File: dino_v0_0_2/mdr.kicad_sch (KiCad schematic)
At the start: 12 parts, among them SW2 SW_Push, SW3 SW_Push, U18 74LS373, U22 74LS121, U23 74LS244N, U25 74LS245, U34 74LS373, U36 74LS73, U37 74LS04, U38 74LS02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

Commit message: Schematic Update
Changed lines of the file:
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@@
 	)
 	(junction
+		(at 125.73 78.74)
+		(diameter 0)
+		(color 0 0 0 0)
+	)
+	(junction
 		(at 194.31 26.67)
 		(diameter 0)
@@
 	)
 	(junction
-		(at 240.03 72.39)
-		(diameter 0)
-		(color 0 0 0 0)
-	)
-	(junction
 		(at 115.57 78.74)
 		(diameter 0)
@@
 	)
 	(junction
-		(at 186.69 132.08)
-		(diameter 0)
-		(color 0 0 0 0)
-	)
-	(junction
 		(at 83.82 105.41)
 		(diameter 0)
@@
 	)
 	(junction
-		(at 173.99 26.67)
+		(at 128.27 41.91)
 		(diameter 0)
 		(color 0 0 0 0)
 	)
 	(junction
-		(at 128.27 41.91)
+		(at 203.2 76.2)
 		(diameter 0)
 		(color 0 0 0 0)
@@
 	)
 	(junction
-		(at 214.63 87.63)
+		(at 128.27 46.99)
 		(diameter 0)
 		(color 0 0 0 0)
 	)
 	(junction
-		(at 128.27 46.99)
+		(at 128.27 72.39)
 		(diameter 0)
 		(color 0 0 0 0)
 	)
 	(junction
-		(at 128.27 72.39)
+		(at 194.31 72.39)
 		(diameter 0)
 		(color 0 0 0 0)
@@
 	(wire
 		(pts
-			(xy 173.99 91.44) (xy 173.99 26.67)
-		)
-		(stroke
-			(width 0)
-			(type default)
-		)
-	)
-	(wire
-		(pts
 			(xy 199.39 109.22) (xy 207.01 109.22)
 		)
@@
 	(wire
 		(pts
-			(xy 214.63 87.63) (xy 217.17 87.63)
+			(xy 203.2 81.28) (xy 205.74 81.28)
 		)
 		(stroke
@@
 	(wire
 		(pts
-			(xy 167.64 26.67) (xy 173.99 26.67)
-		)
-		(stroke
-			(width 0)
-			(type default)
-		)
-	)
-	(wire
-		(pts
 			(xy 121.92 132.08) (xy 127 132.08)
 		)
@@
 	(wire
 		(pts
-			(xy 173.99 26.67) (xy 194.31 26.67)
+			(xy 167.64 26.67) (xy 194.31 26.67)
 		)
 		(stroke
@@
 	(wire
 		(pts
+			(xy 203.2 76.2) (xy 203.2 81.28)
+		)
+		(stroke
+			(width 0)
+			(type default)
+		)
+	)
+	(wire
+		(pts
+			(xy 203.2 76.2) (xy 214.63 76.2)
+		)
+		(stroke
+			(width 0)
+			(type default)
+		)
+	)
+	(wire
+		(pts
 			(xy 67.31 146.05) (xy 142.24 146.05)
 		)
@@
 		)
 	)
+	(wire
+		(pts
+			(xy 179.07 62.23) (xy 179.07 76.2)
+		)
+		(stroke
+			(width 0)
+			(type default)
+		)
+	)
 	(bus
 		(pts
@@
 	(wire
 		(pts
+			(xy 186.69 78.74) (xy 186.69 91.44)
+		)
+		(stroke
+			(width 0)
+			(type default)
+		)
+	)
+	(wire
+		(pts
+			(xy 214.63 64.77) (xy 214.63 76.2)
+		)
+		(stroke
+			(width 0)
+			(type default)
+		)
+	)
+	(wire
+		(pts
 			(xy 170.18 44.45) (xy 181.61 44.45)
 		)
@@
 	(wire
 		(pts
-			(xy 240.03 132.08) (xy 240.03 72.39)
+			(xy 170.18 104.14) (xy 173.99 104.14)
 		)
 		(stroke
@@
 	(wire
 		(pts
-			(xy 170.18 104.14) (xy 173.99 104.14)
+			(xy 207.01 46.99) (xy 214.63 46.99)
 		)
 		(stroke
@@
 	(wire
 		(pts
-			(xy 207.01 46.99) (xy 214.63 46.99)
+			(xy 105.41 82.55) (xy 105.41 78.74)
 		)
 		(stroke
@@
 	(wire
 		(pts
-			(xy 105.41 82.55) (xy 105.41 78.74)
+			(xy 142.24 72.39) (xy 194.31 72.39)
 		)
 		(stroke
@@
 		)
 	)
-	(wire
-		(pts
-			(xy 179.07 62.23) (xy 179.07 87.63)
-		)
-		(stroke
-			(width 0)
-			(type default)
-		)
-	)
 	(bus
 		(pts
@@
 	(wire
 		(pts
+			(xy 125.73 78.74) (xy 186.69 78.74)
+		)
+		(stroke
+			(width 0)
+			(type default)
+		)
+	)
+	(wire
+		(pts
 			(xy 123.19 62.23) (xy 123.19 63.5)
 		)
@@
 	(wire
 		(pts
-			(xy 179.07 87.63) (xy 214.63 87.63)
+			(xy 179.07 76.2) (xy 203.2 76.2)
 		)
 		(stroke
@@
 	(wire
 		(pts
-			(xy 214.63 64.77) (xy 214.63 87.63)
-		)
-		(stroke
-			(width 0)
-			(type default)
-		)
-	)
-	(wire
-		(pts
-			(xy 186.69 91.44) (xy 173.99 91.44)
-		)
-		(stroke
-			(width 0)
-			(type default)
-		)
-	)
-	(wire
-		(pts
 			(xy 252.73 41.91) (xy 259.08 41.91)
 		)
@@
 	(wire
 		(pts
-			(xy 186.69 132.08) (xy 240.03 132.08)
-		)
-		(stroke
-			(width 0)
-			(type default)
-		)
-	)
-	(wire
-		(pts
 			(xy 83.82 105.41) (xy 105.41 105.41)
 		)
@@
 	)
 	(label "~{MDR_OUT}"
-		(at 217.17 87.63 0)
+		(at 205.74 81.28 0)
 		(effects
 			(font
@@
 		(on_board yes)
 		(dnp no)
-		(fields_autoplaced yes)
 		(property "Reference" "U34"
 			(at 188.8333 91.44 0)

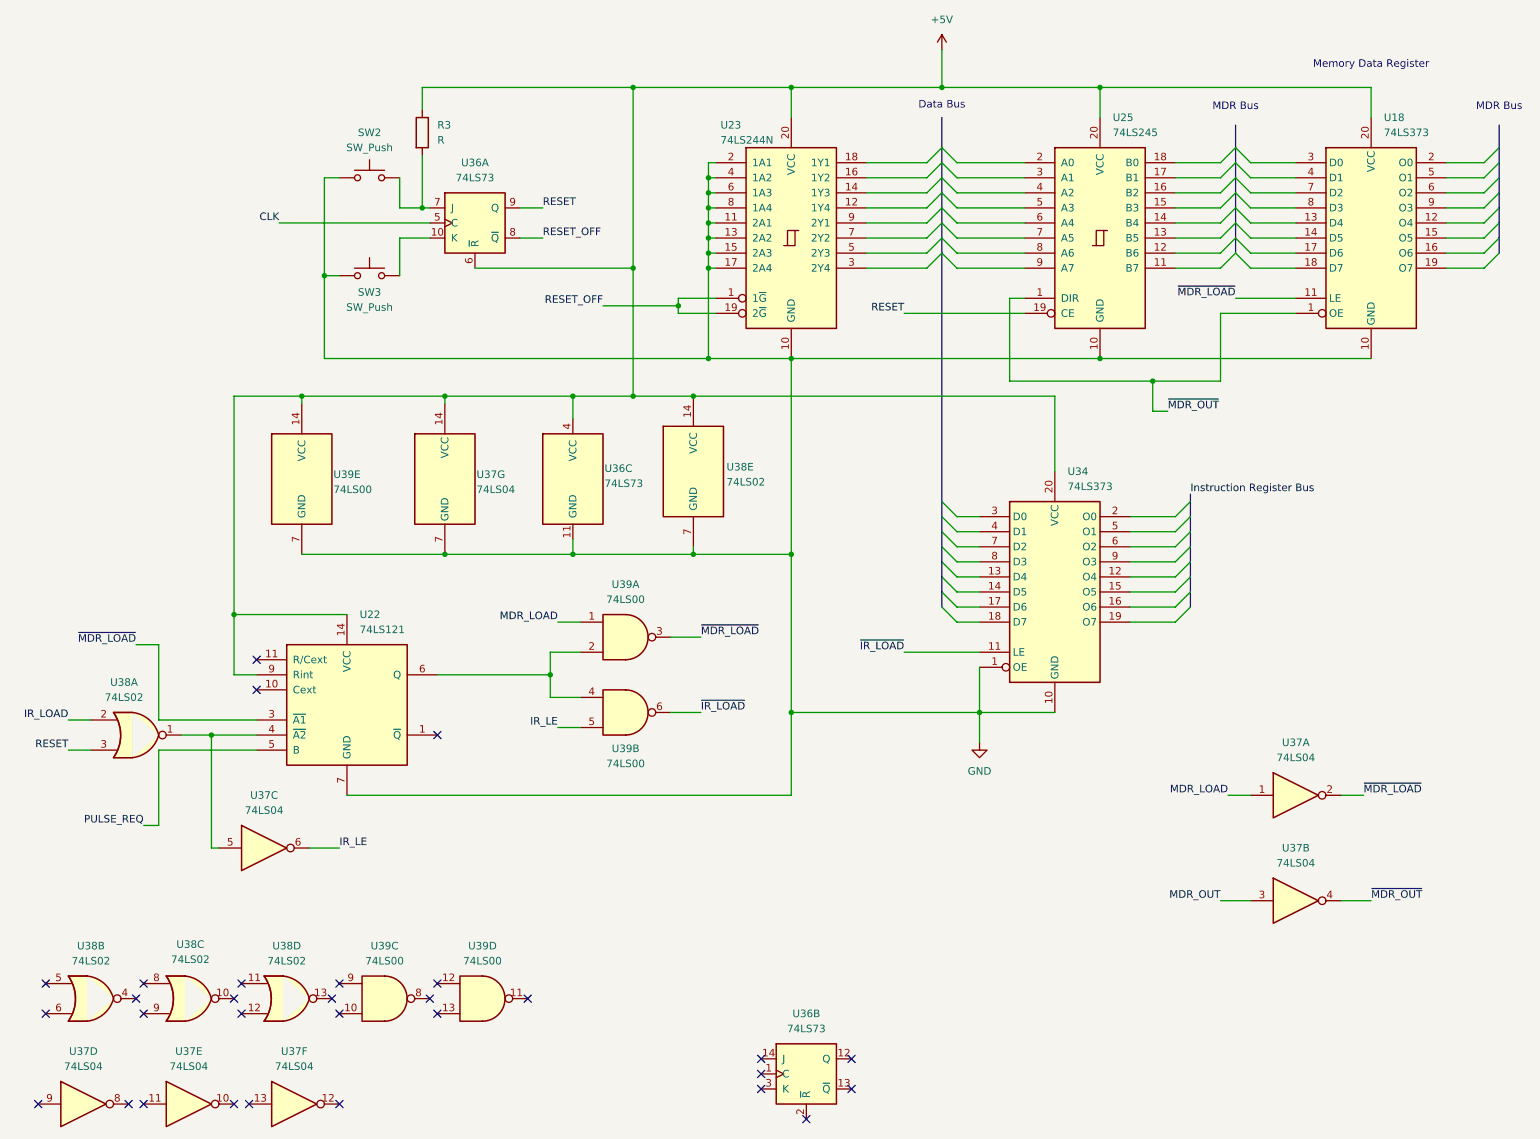
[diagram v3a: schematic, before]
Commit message: Memory Register Module Update
With some previous learnings on the 74LS121, the MDR Module has been re-sketched to better trigger the '121 and create an intra phase latch. This should allow the data bus to stabilize before the the register's latch the data.
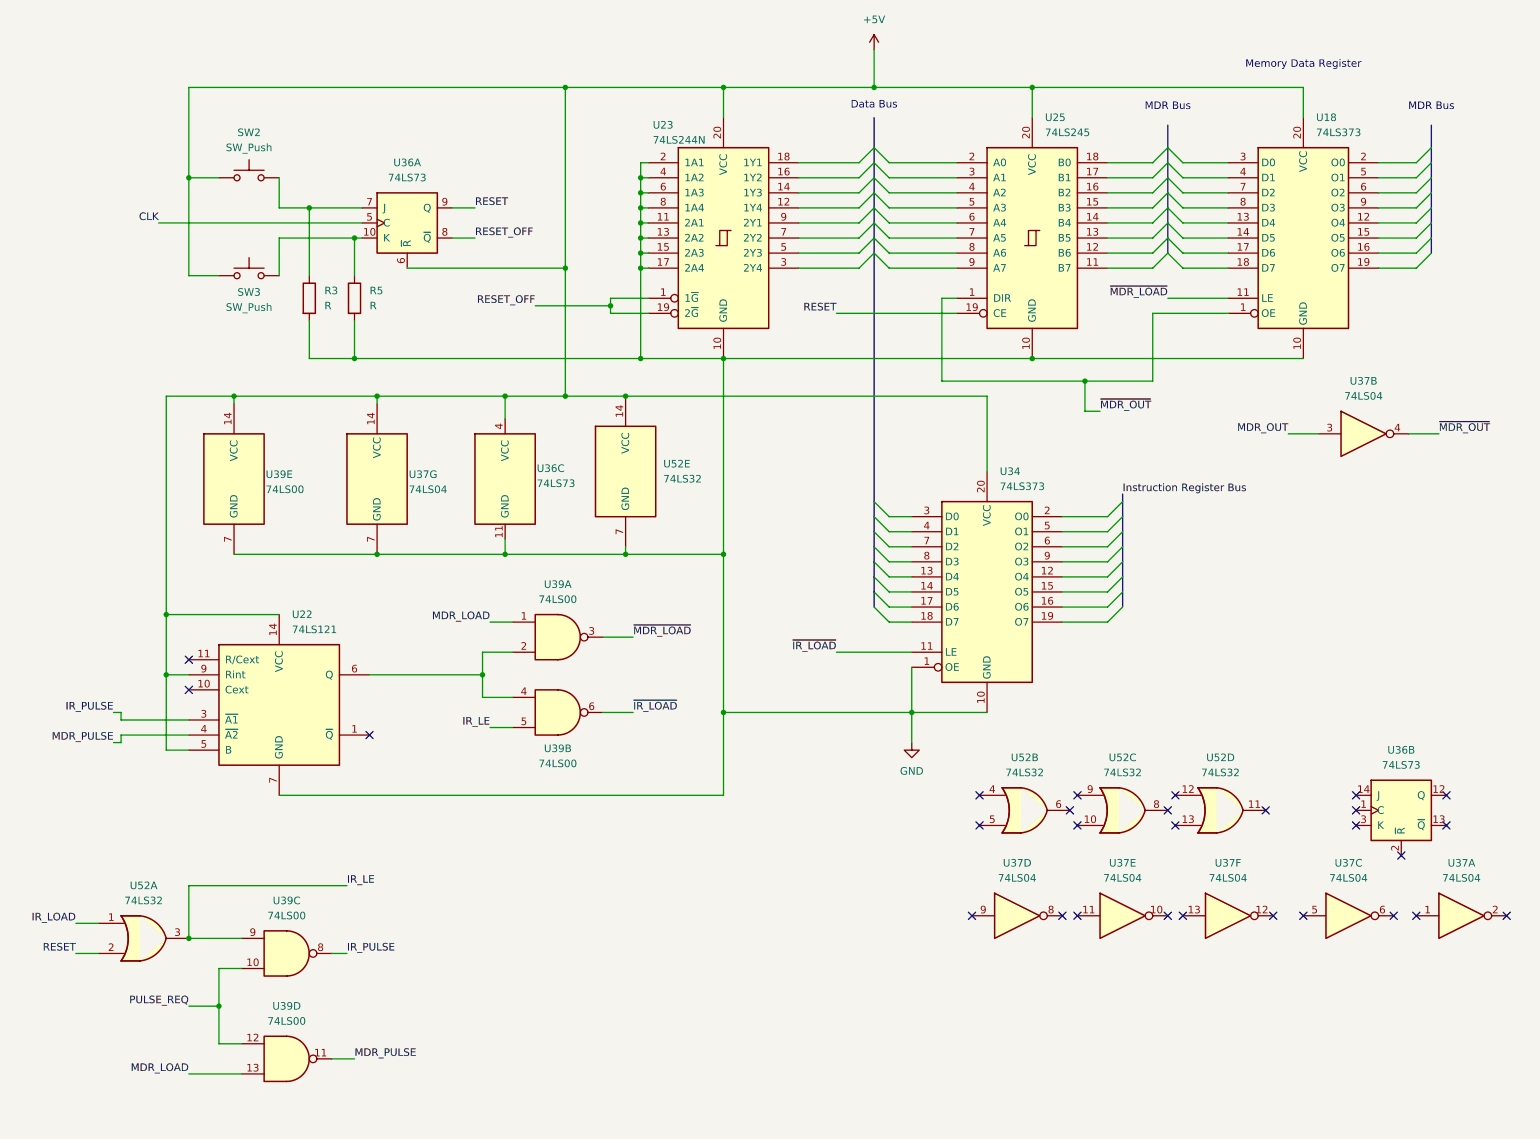
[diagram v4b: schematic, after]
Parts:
- removed U38: 74LS02, symbol 74xx:74LS02
- added R5: R, symbol Device:R
- added U52: 74LS32, symbol 74xx:74LS32
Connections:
- net +5V: now also SW2.1, SW3.1, U22.5 (B), U52.14 (VCC); no longer R3.1
- net GND: now also R3.2, R5.2, U52.7 (GND); no longer SW2.1, SW3.1
- net IR_LE: now also U39.9, U52.3; no longer U37.6
- net IR_LOAD: now also U52.1
- net MDR_LOAD: now also U39.13; no longer U37.1
- net PULSE_REQ: now also U39.10, U39.12; no longer U22.5 (B)
- net RESET: now also U52.2
- net ~{MDR_LOAD}: no longer U22.3 (~{A1}), U37.2
- net at U37.5: no longer U22.4 (~{A2})
- net at SW3.2, U36.10 (K): now also R5.1
- net at SW2.2, U36.7 (J): now also R3.1; no longer R3.2
- net MDR_PULSE: now reaches U39.11
- net MDR_PULSE: now also U22.4 (~{A2})
- net IR_PULSE: now reaches U39.8
- net IR_PULSE: now also U22.3 (~{A1})
- no-connect marks 30 -> 28
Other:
- moved on the sheet: R3, SW2, SW3, U18, U22, U23, U25, U34, U36A, U36B, U36C, U37A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

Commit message: Updates microcontroller schematic from 74LS73 to 74LS74
Replaces 74LS73 JK flip-flop components with 74LS74 D flip-flops
for improved synchronization in the circuit. Adjusts pin
mappings accordingly and updates datasheets and descriptions.
Removes auto-saved schematic file.

Adds capacitor and resistor components to the schematic for
circuit completion. Includes new images and documentation for
reference.
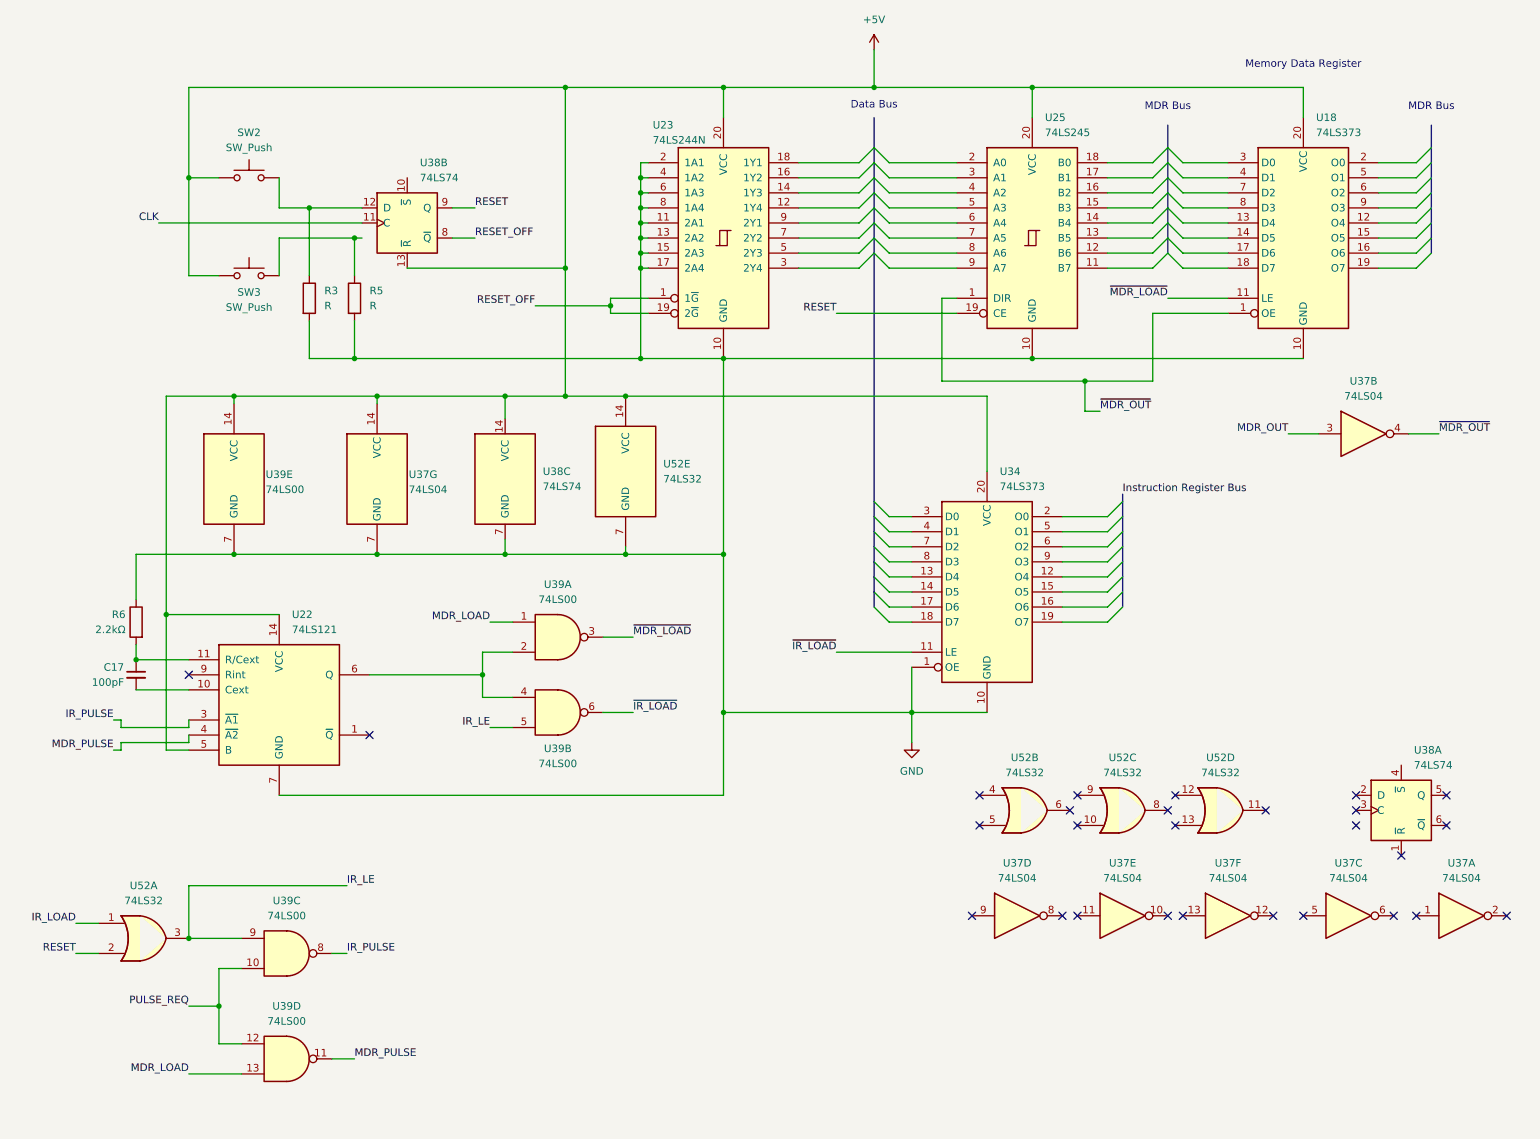
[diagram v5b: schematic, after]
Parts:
- removed U36: 74LS73, symbol 74xx:74LS73
- added C17: 100pF, symbol Device:C_Small
- added R6: 2.2kΩ, symbol Device:R
- added U38: 74LS74, symbol 74xx:74LS74
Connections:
- net +5V: now also U38.13 (~{R}), U38.14 (VCC); no longer U22.9 (Rint)
- net CLK: now also U38.11 (C)
- net GND: now also R6.1, U38.7 (GND)
- net RESET: now also U38.9 (Q)
- net RESET_OFF: now also U38.8 (~{Q})
- net at R3.1, SW2.2: now also U38.12 (D)
- net at U22.10 (Cext): now also C17.2
- net at U22.11 (R/Cext): now also C17.1, R6.2
- no-connect marks 28 -> 27
